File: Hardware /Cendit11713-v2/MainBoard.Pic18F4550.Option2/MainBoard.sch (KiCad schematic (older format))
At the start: 88 parts, among them CON1 POWER_BUS, CON2 ICSP_CON, CON3 USB_CON, J1 RESET_CON, J2 SATA_PLUG _22P_SMT, J4 SATA_PLUG _22P_SMT, P1 DEBUG_HEADER_21P, P2 DEBUG_HEADER_21P, Q1 2N2222, U1 PIC18F4550-I/P, U3 PCF85263A, Y1 Crystal, Y2 32.768KHZ

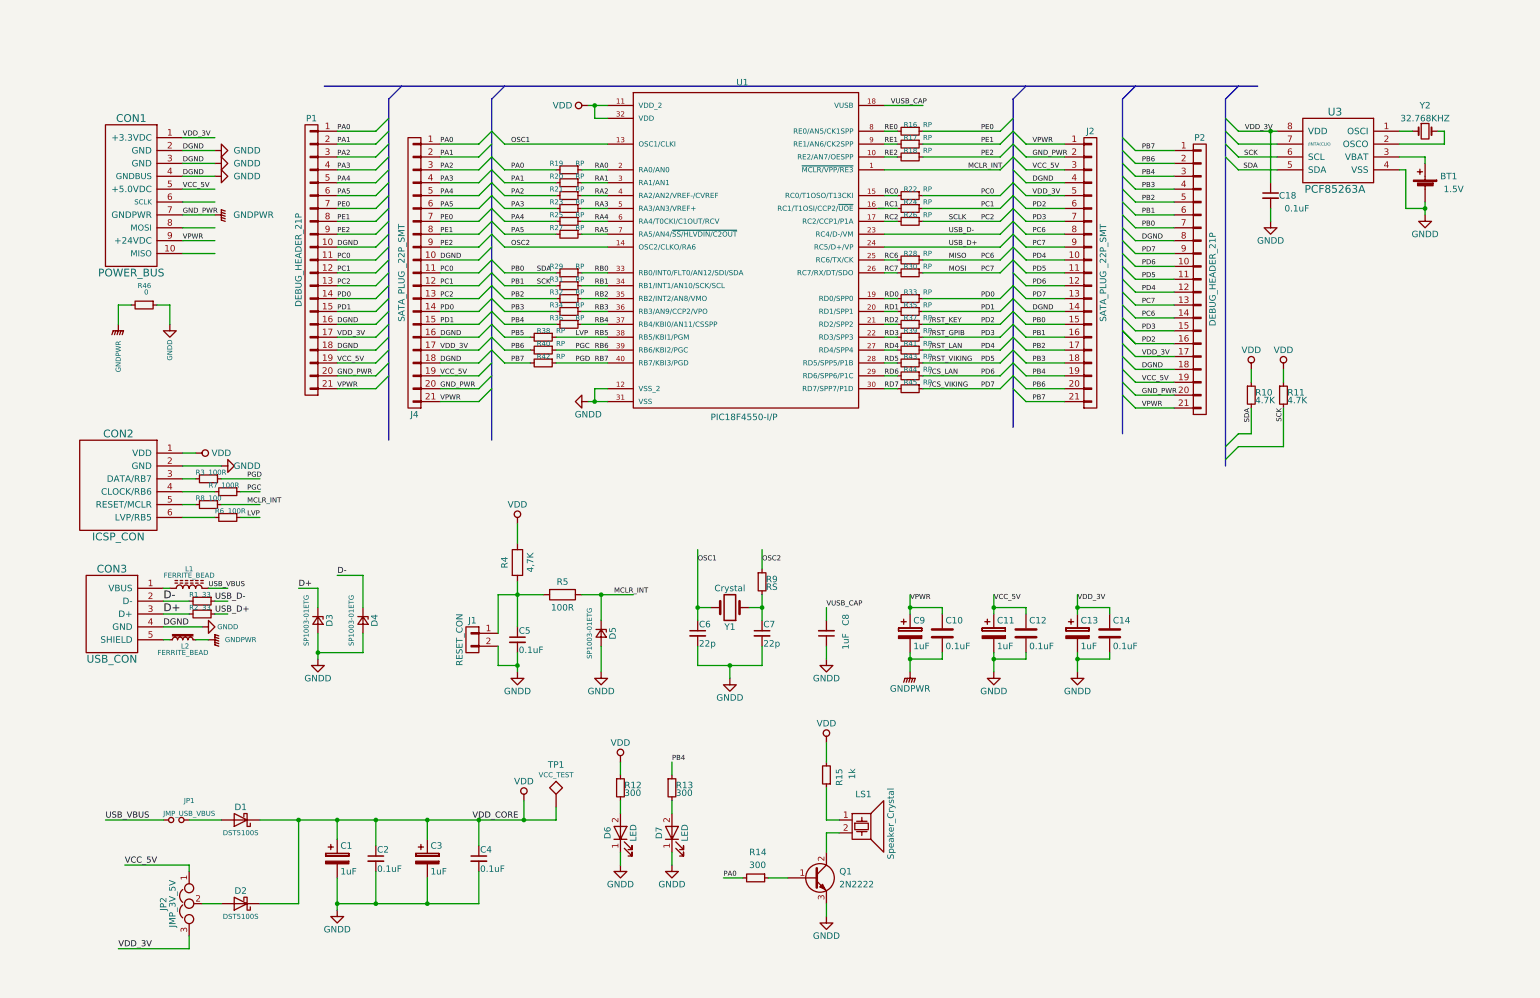
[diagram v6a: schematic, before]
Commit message: En CenditLab + Cendit11713
  - Edicion de PCB tarjeta madre
  - Revision de PCB expansor Viking
  - Archivos gerber generados

  - Edicion de clases UI
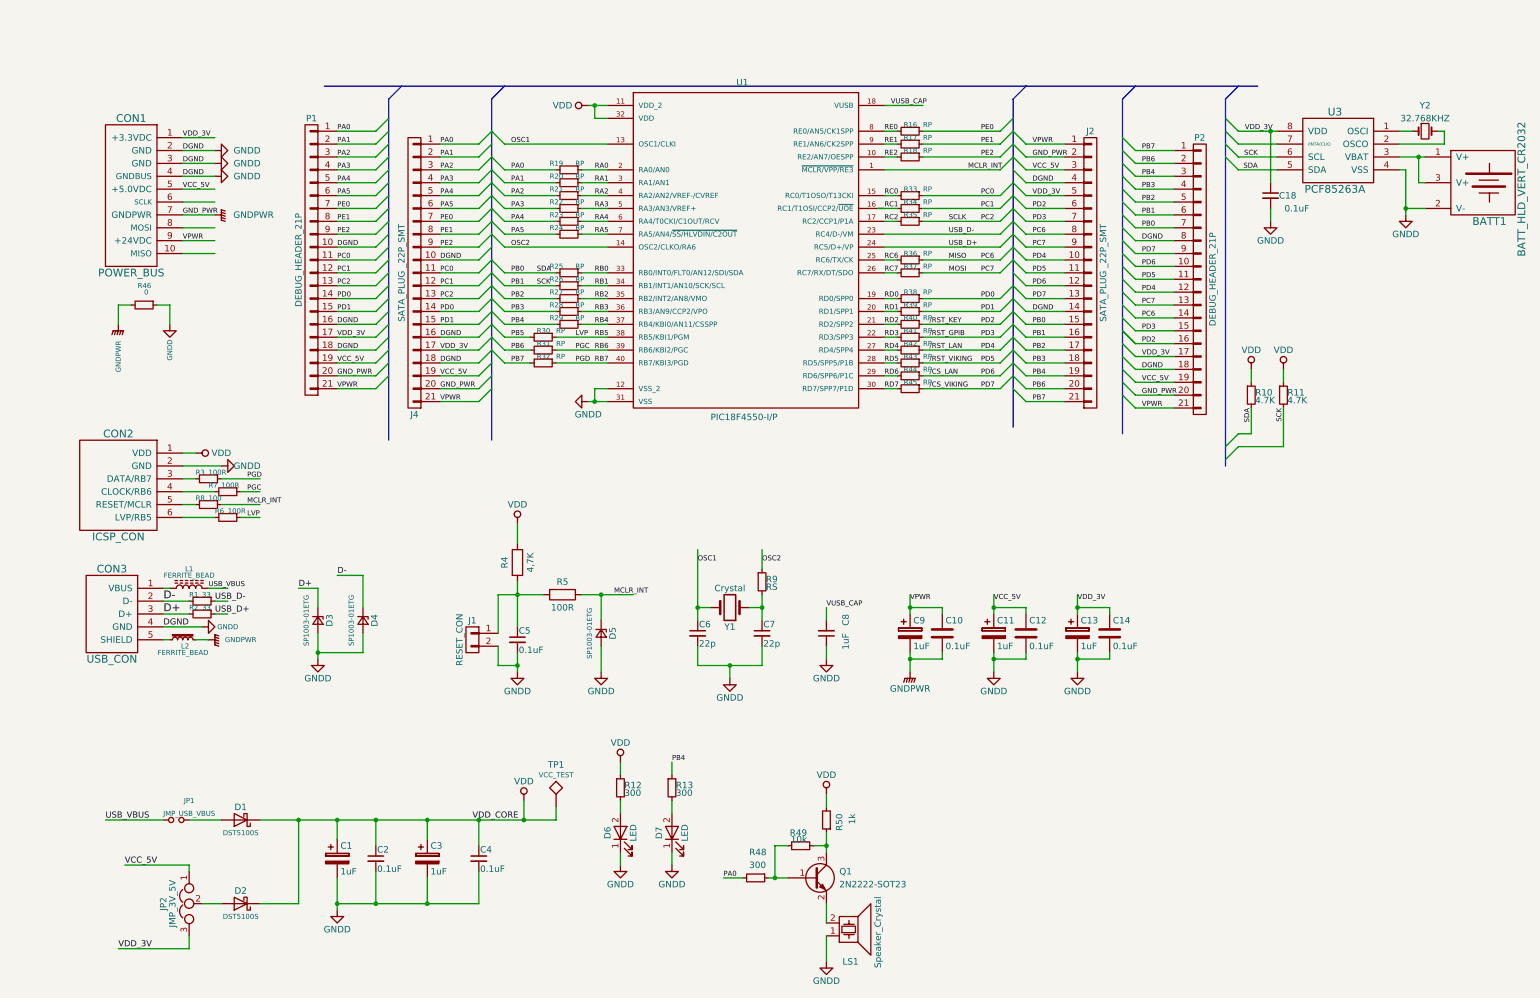
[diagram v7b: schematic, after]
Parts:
- removed BT1: 1.5V, symbol Battery_Cell
- removed Q1: 2N2222, TO_SOT_Packages_SMD:TSOT-23, symbol Q_NPN_BCE
- added BATT1: BATT_HLD_VERT_CR2032, CenditFootprints:BATTERY_HOLDER_VERT_CR2032, symbol BATT_HLD_VERT_CR2032
- added Q1: 2N2222-SOT23, symbol Q_NPN_BEC
- added R49: 10k, Resistors_SMD:R_0603_HandSoldering, symbol R_Small
- CON1: footprint (none) -> Pin_Headers:Pin_Header_Straight_2x05_Pitch2.54mm
- R16, R17, R18, R19, R20, R21, R43, R44, R45: footprint Resistors_SMD:R_0603_HandSoldering -> Resistors_SMD:R_0805_HandSoldering
- R22: renamed from R23; footprint Resistors_SMD:R_0603_HandSoldering -> Resistors_SMD:R_0805_HandSoldering
- R23: renamed from R25; footprint Resistors_SMD:R_0603_HandSoldering -> Resistors_SMD:R_0805_HandSoldering
- R24: renamed from R27; footprint Resistors_SMD:R_0603_HandSoldering -> Resistors_SMD:R_0805_HandSoldering
- R25: renamed from R29; footprint Resistors_SMD:R_0603_HandSoldering -> Resistors_SMD:R_0805_HandSoldering
- R26: renamed from R31; footprint Resistors_SMD:R_0603_HandSoldering -> Resistors_SMD:R_0805_HandSoldering
- R27: renamed from R32; footprint Resistors_SMD:R_0603_HandSoldering -> Resistors_SMD:R_0805_HandSoldering
- R28: renamed from R34; footprint Resistors_SMD:R_0603_HandSoldering -> Resistors_SMD:R_0805_HandSoldering
- R29: renamed from R36; footprint Resistors_SMD:R_0603_HandSoldering -> Resistors_SMD:R_0805_HandSoldering
- R30: renamed from R38; footprint Resistors_SMD:R_0603_HandSoldering -> Resistors_SMD:R_0805_HandSoldering
- R31: renamed from R40; footprint Resistors_SMD:R_0603_HandSoldering -> Resistors_SMD:R_0805_HandSoldering
- R32: renamed from R42; footprint Resistors_SMD:R_0603_HandSoldering -> Resistors_SMD:R_0805_HandSoldering
- R33: renamed from R22; footprint Resistors_SMD:R_0603_HandSoldering -> Resistors_SMD:R_0805_HandSoldering
- R34: renamed from R24; footprint Resistors_SMD:R_0603_HandSoldering -> Resistors_SMD:R_0805_HandSoldering
- R35: renamed from R26; footprint Resistors_SMD:R_0603_HandSoldering -> Resistors_SMD:R_0805_HandSoldering
- R36: renamed from R28; footprint Resistors_SMD:R_0603_HandSoldering -> Resistors_SMD:R_0805_HandSoldering
- R37: renamed from R30; footprint Resistors_SMD:R_0603_HandSoldering -> Resistors_SMD:R_0805_HandSoldering
- R38: renamed from R33; footprint Resistors_SMD:R_0603_HandSoldering -> Resistors_SMD:R_0805_HandSoldering
- R39: renamed from R35; footprint Resistors_SMD:R_0603_HandSoldering -> Resistors_SMD:R_0805_HandSoldering
- R40: renamed from R37; footprint Resistors_SMD:R_0603_HandSoldering -> Resistors_SMD:R_0805_HandSoldering
- R41: renamed from R39; footprint Resistors_SMD:R_0603_HandSoldering -> Resistors_SMD:R_0805_HandSoldering
- R42: renamed from R41; footprint Resistors_SMD:R_0603_HandSoldering -> Resistors_SMD:R_0805_HandSoldering
- R48: renamed from R14; footprint Resistors_SMD:R_0805_HandSoldering -> Resistors_SMD:R_0603_HandSoldering
- R50: renamed from R15; footprint Resistors_SMD:R_0805_HandSoldering -> Resistors_SMD:R_0603_HandSoldering
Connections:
- wire segments 292 -> 293
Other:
- moved on the sheet: LS1, R50
